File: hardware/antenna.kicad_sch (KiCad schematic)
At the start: 8 parts

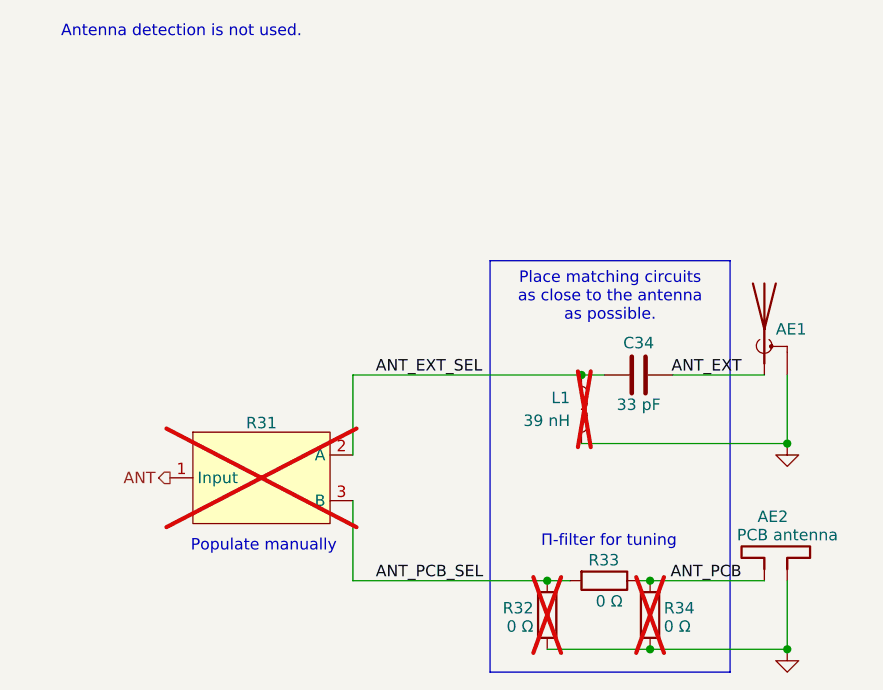
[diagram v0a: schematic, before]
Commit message: HW: Update 0hm choice
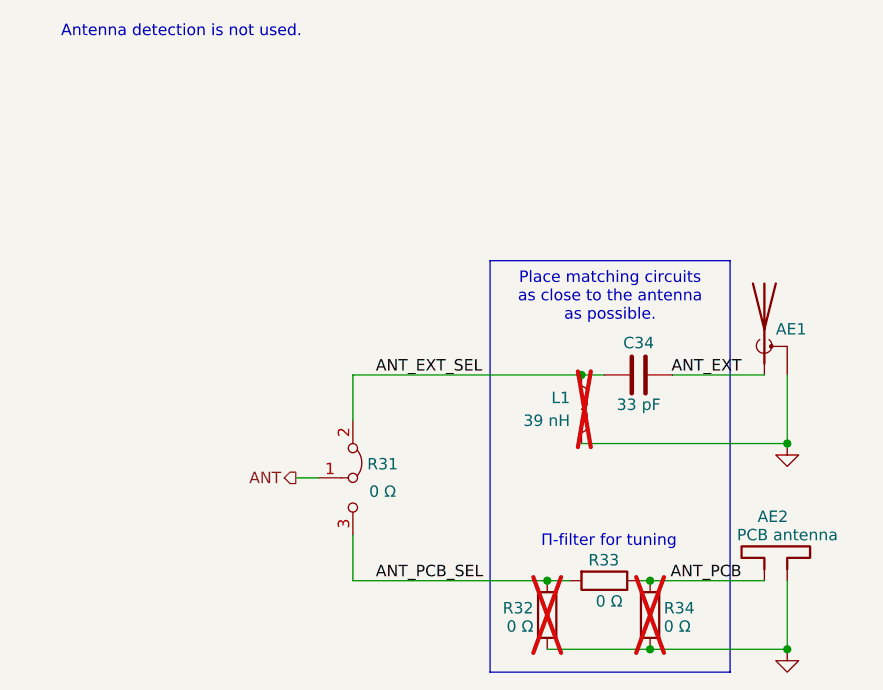
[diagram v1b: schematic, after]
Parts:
- R31: value ~ -> 0 Ω; now fitted; now in the parts list
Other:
- note removed: "Populate manually"
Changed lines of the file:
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@@
 	(wire
 		(pts
-			(xy 134.62 119.38) (xy 123.19 119.38)
+			(xy 101.6 106.68) (xy 101.6 111.76)
 		)
 		(stroke
@@
 	(wire
 		(pts
-			(xy 149.86 111.76) (xy 149.86 119.38)
+			(xy 134.62 119.38) (xy 123.19 119.38)
 		)
 		(stroke
@@
 	(wire
 		(pts
-			(xy 101.6 97.79) (xy 101.6 88.9)
+			(xy 149.86 111.76) (xy 149.86 119.38)
 		)
 		(stroke
@@
 	(wire
 		(pts
+			(xy 95.25 100.33) (xy 97.79 100.33)
+		)
+		(stroke
+			(width 0)
+			(type default)
+		)
+	)
+	(wire
+		(pts
 			(xy 149.86 96.52) (xy 127 96.52)
 		)
@@
 	(wire
 		(pts
-			(xy 147.32 111.76) (xy 134.62 111.76)
+			(xy 101.6 88.9) (xy 101.6 93.98)
 		)
 		(stroke
@@
 	(wire
 		(pts
-			(xy 125.73 111.76) (xy 123.19 111.76)
+			(xy 147.32 111.76) (xy 134.62 111.76)
 		)
 		(stroke
@@
 	(wire
 		(pts
-			(xy 101.6 88.9) (xy 127 88.9)
+			(xy 125.73 111.76) (xy 123.19 111.76)
 		)
 		(stroke
@@
 	(wire
 		(pts
-			(xy 147.32 88.9) (xy 137.16 88.9)
+			(xy 101.6 88.9) (xy 127 88.9)
 		)
 		(stroke
@@
 	(wire
 		(pts
-			(xy 101.6 111.76) (xy 101.6 102.87)
+			(xy 147.32 88.9) (xy 137.16 88.9)
 		)
 		(stroke
@@
 		)
 	)
-	(text "Populate manually"
-		(exclude_from_sim no)
-		(at 91.694 107.95 0)
-		(effects
-			(font
-				(size 1.27 1.27)
-			)
-		)
-	)
 	(text "Π-filter for tuning"
 		(exclude_from_sim no)
@@
 	(hierarchical_label "ANT"
 		(shape output)
-		(at 81.28 100.33 180)
+		(at 95.25 100.33 180)
 		(fields_autoplaced yes)
 		(effects
@@
 	(symbol
 		(lib_id "perfect_footprints:0hm_choice")
-		(at 91.44 100.33 0)
+		(at 101.6 100.33 270)
 		(unit 1)
 		(exclude_from_sim no)
-		(in_bom no)
+		(in_bom yes)
 		(on_board yes)
-		(dnp yes)
+		(dnp no)
 		(property "Reference" "R31"
-			(at 91.44 94.234 0)
+			(at 104.902 98.806 90)
 			(effects
 				(font
@@
 			)
 		)
-		(property "Value" "~"
-			(at 91.44 93.98 0)
+		(property "Value" "0 Ω"
+			(at 104.902 101.854 90)
 			(effects
 				(font
@@
 		)
 		(property "Footprint" "perfect_footprints:0hm_choice"
-			(at 91.44 108.458 0)
+			(at 93.472 100.33 0)
 			(effects
 				(font
@@
 		)
 		(property "Datasheet" ""
-			(at 86.36 96.52 0)
+			(at 105.41 95.25 0)
 			(effects
 				(font
@@
 		)
 		(property "Description" ""
-			(at 86.36 96.52 0)
+			(at 105.41 95.25 0)
 			(effects
 				(font

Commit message: HW: Update BOM
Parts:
- AE2: Digi-Key Part Number (none) -> -; Manufacturer (none) -> -; Manufacturer Part Number (none) -> -
- R31: Digi-Key Part Number (none) -> 311-0.0JRCT-ND; Manufacturer (none) -> YAGEO; Manufacturer Part Number (none) -> RC0402JR-070RL
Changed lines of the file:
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@@
+			)
+		)
+		(property "Digi-Key Part Number" "-"
+			(at 147.32 106.68 0)
+			(effects
+				(font
+					(size 1.27 1.27)
+				)
+				(hide yes)
+			)
+		)
+		(property "Manufacturer" "-"
+			(at 147.32 106.68 0)
+			(effects
+				(font
+					(size 1.27 1.27)
+				)
+				(hide yes)
+			)
+		)
+		(property "Manufacturer Part Number" "-"
+			(at 147.32 106.68 0)
+			(effects
+				(font
+					(size 1.27 1.27)
+				)
+				(hide yes)
 			)
 		)
@@
 			(effects
 				(font
+					(size 1.27 1.27)
+				)
+				(hide yes)
+			)
+		)
+		(property "Digi-Key Part Number" "311-0.0JRCT-ND"
+			(at 101.6 100.33 0)
+			(effects
+				(font
+					(size 1.27 1.27)
+				)
+				(hide yes)
+			)
+		)
+		(property "Manufacturer" "YAGEO"
+			(at 101.6 100.33 0)
+			(effects
+				(font
+					(size 1.27 1.27)
+				)
+				(hide yes)
+			)
+		)
+		(property "Manufacturer Part Number" "RC0402JR-070RL"
+			(at 101.6 100.33 0)
+			(effects
+				(font

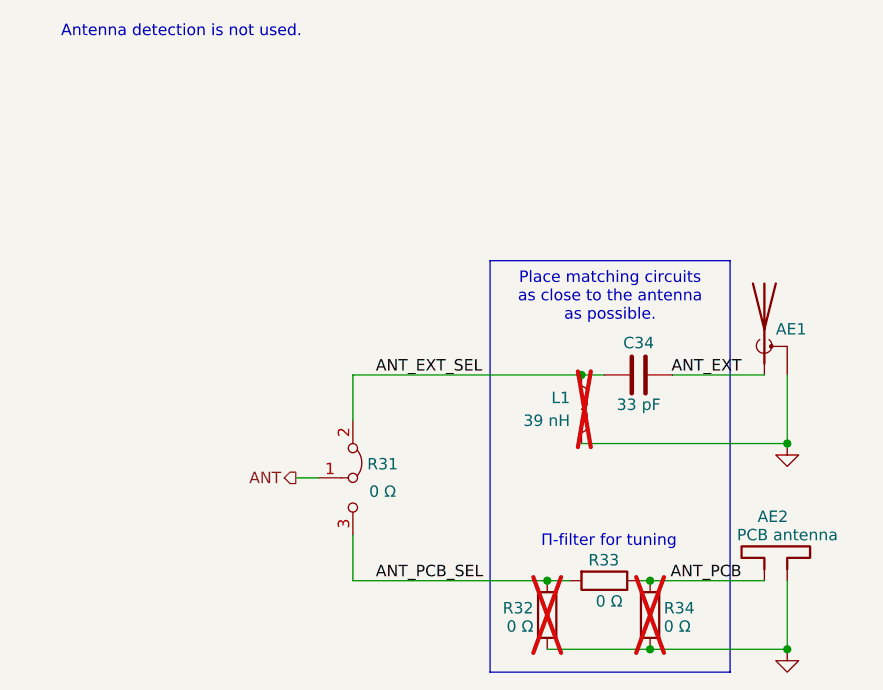
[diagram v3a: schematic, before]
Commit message: HW: Connect +BATT to MCU
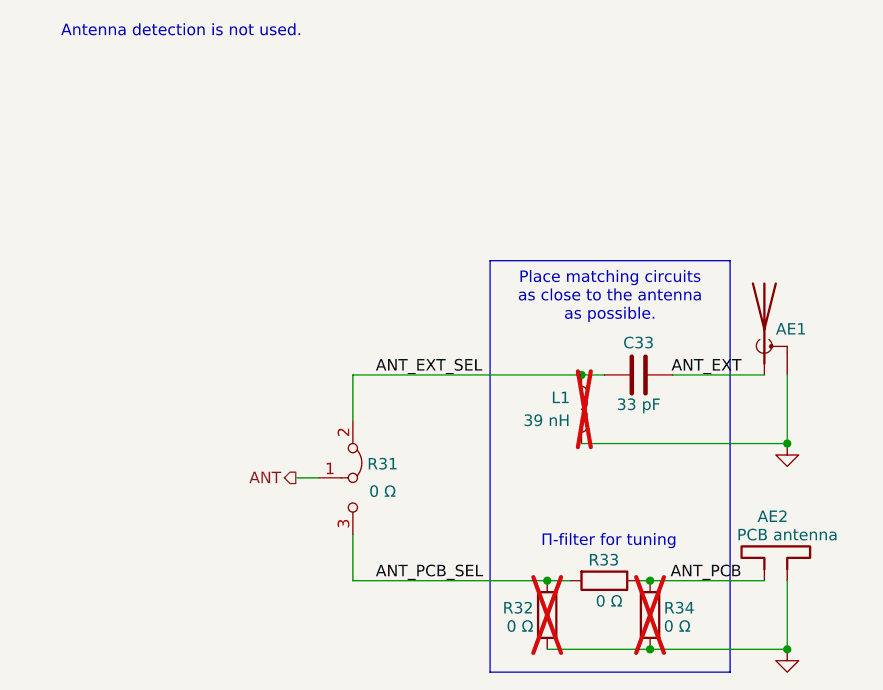
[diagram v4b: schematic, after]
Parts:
- renumbered C34 to C33
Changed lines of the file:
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@@
 	(title_block
 		(title "Iida devkit")
-		(date "2024-09-22")
-		(rev "v4.1.0")
+		(date "2024-09-25")
+		(rev "v4.2.0")
 	)
 	(junction
@@
 		(on_board yes)
 		(dnp no)
-		(property "Reference" "C34"
+		(property "Reference" "C33"
 			(at 133.35 85.344 90)
 			(effects
@@
 			(project "iida_devkit"
 				(path "/b12a6e25-97fb-4aba-bc96-af8db389bb9a/6e456e95-dbda-43fc-b148-815c3be21ba0"
-					(reference "C34")
+					(reference "C33")
 					(unit 1)
 				)

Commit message: HW: Update components
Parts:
- C33: Digi-Key Part Number 490-5936-1-ND -> 732-7472-1-ND; Manufacturer Murata Electronics -> Würth Elektronik; Manufacturer Part Number GRM1555C1H330JA01D -> 885012005058
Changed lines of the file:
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@@
 			)
 		)
-		(property "Digi-Key Part Number" "490-5936-1-ND"
+		(property "Digi-Key Part Number" "732-7472-1-ND"
 			(at 133.35 88.9 0)
 			(effects
@@
 			)
 		)
-		(property "Manufacturer" "Murata Electronics"
+		(property "Manufacturer" "Würth Elektronik"
 			(at 133.35 88.9 0)
 			(effects
@@
 			)
 		)
-		(property "Manufacturer Part Number" "GRM1555C1H330JA01D"
+		(property "Manufacturer Part Number" "885012005058"
 			(at 133.35 88.9 0)
 			(effects

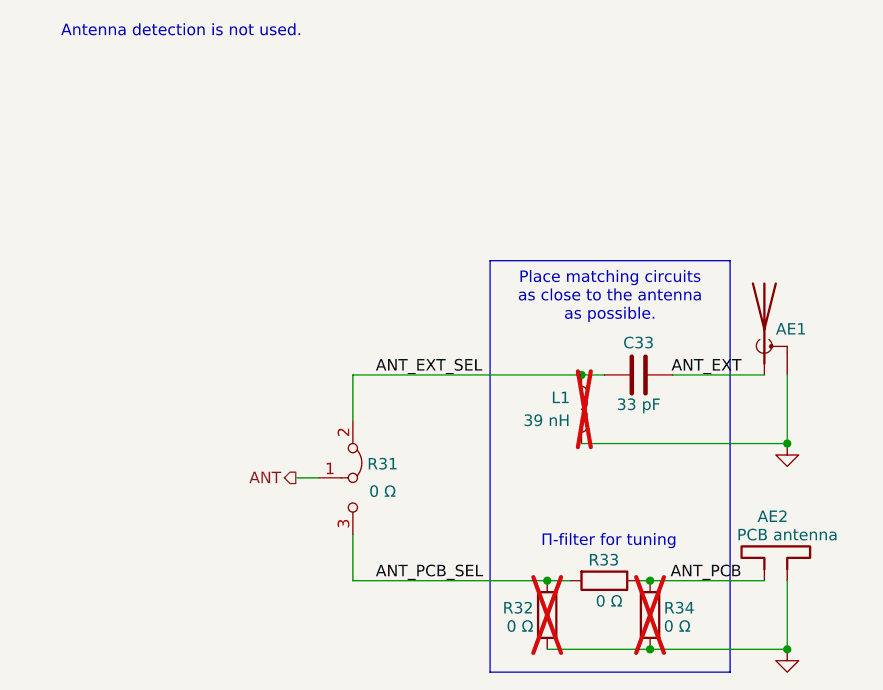
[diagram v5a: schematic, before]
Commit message: HW: Update VBAT, schema and layout
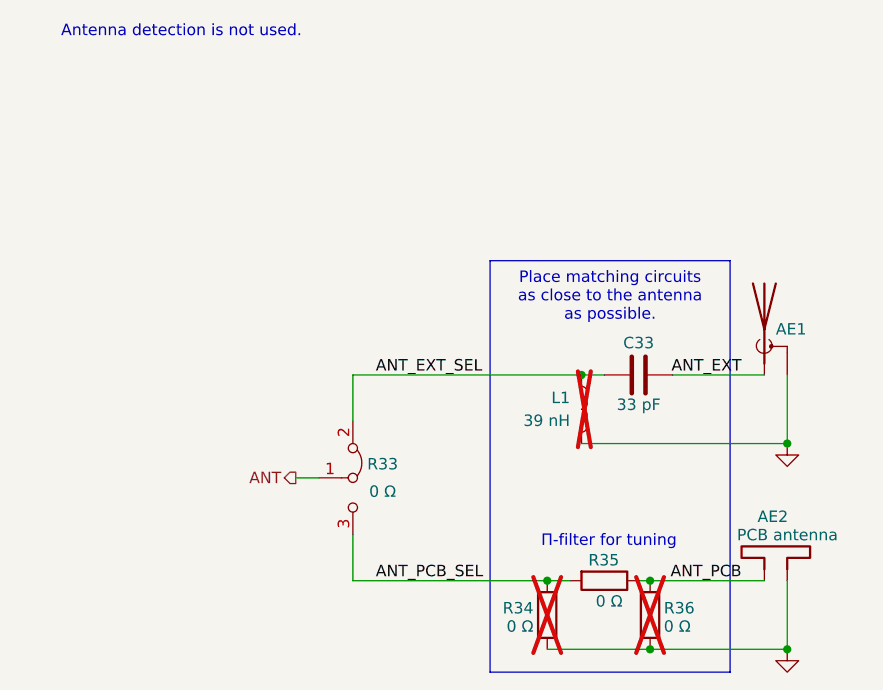
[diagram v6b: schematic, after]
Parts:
- renumbered R31 to R33, R32 to R34, R33 to R35, R34 to R36
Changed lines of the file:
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@@
 		(on_board yes)
 		(dnp no)
-		(property "Reference" "R33"
+		(property "Reference" "R35"
 			(at 127.762 109.474 90)
 			(effects
@@
 			(project "iida_devkit"
 				(path "/b12a6e25-97fb-4aba-bc96-af8db389bb9a/6e456e95-dbda-43fc-b148-815c3be21ba0"
-					(reference "R33")
+					(reference "R35")
 					(unit 1)
 				)
@@
 		(on_board yes)
 		(dnp yes)
-		(property "Reference" "R32"
+		(property "Reference" "R34"
 			(at 121.666 114.808 0)
 			(effects
@@
 			(project "iida_devkit"
 				(path "/b12a6e25-97fb-4aba-bc96-af8db389bb9a/6e456e95-dbda-43fc-b148-815c3be21ba0"
-					(reference "R32")
+					(reference "R34")
 					(unit 1)
 				)
@@
 		(on_board yes)
 		(dnp yes)
-		(property "Reference" "R34"
+		(property "Reference" "R36"
 			(at 136.144 114.808 0)
 			(effects
@@
 			(project "iida_devkit"
 				(path "/b12a6e25-97fb-4aba-bc96-af8db389bb9a/6e456e95-dbda-43fc-b148-815c3be21ba0"
-					(reference "R34")
+					(reference "R36")
 					(unit 1)
 				)
@@
 		(on_board yes)
 		(dnp no)
-		(property "Reference" "R31"
+		(property "Reference" "R33"
 			(at 104.902 98.806 90)
 			(effects
@@
 			(project ""
 				(path "/b12a6e25-97fb-4aba-bc96-af8db389bb9a/6e456e95-dbda-43fc-b148-815c3be21ba0"
-					(reference "R31")
+					(reference "R33")
 					(unit 1)
 				)

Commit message: HW: Start adding Li-Po support
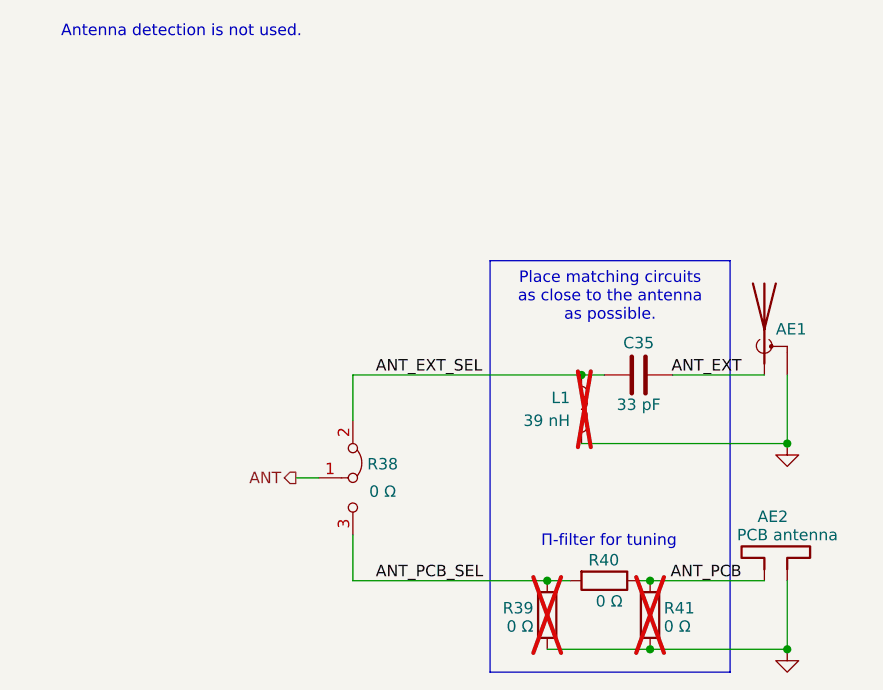
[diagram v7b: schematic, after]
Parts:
- renumbered C33 to C35, R33 to R38, R34 to R39, R35 to R40, R36 to R41
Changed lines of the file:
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@@
 		(on_board yes)
 		(dnp no)
-		(property "Reference" "C33"
+		(property "Reference" "C35"
 			(at 133.35 85.344 90)
 			(effects
@@
 			(project "iida_devkit"
 				(path "/b12a6e25-97fb-4aba-bc96-af8db389bb9a/6e456e95-dbda-43fc-b148-815c3be21ba0"
-					(reference "C33")
+					(reference "C35")
 					(unit 1)
 				)
@@
 		(on_board yes)
 		(dnp no)
-		(property "Reference" "R35"
+		(property "Reference" "R40"
 			(at 127.762 109.474 90)
 			(effects
@@
 			(project "iida_devkit"
 				(path "/b12a6e25-97fb-4aba-bc96-af8db389bb9a/6e456e95-dbda-43fc-b148-815c3be21ba0"
-					(reference "R35")
+					(reference "R40")
 					(unit 1)
 				)
@@
 		(dnp no)
 		(fields_autoplaced yes)
-		(property "Reference" "#PWR029"
+		(property "Reference" "#PWR051"
 			(at 149.86 125.73 0)
 			(effects
@@
 			(project "iida_devkit"
 				(path "/b12a6e25-97fb-4aba-bc96-af8db389bb9a/6e456e95-dbda-43fc-b148-815c3be21ba0"
-					(reference "#PWR029")
+					(reference "#PWR051")
 					(unit 1)
 				)
@@
 		(on_board yes)
 		(dnp yes)
-		(property "Reference" "R34"
+		(property "Reference" "R39"
 			(at 121.666 114.808 0)
 			(effects
@@
 			(project "iida_devkit"
 				(path "/b12a6e25-97fb-4aba-bc96-af8db389bb9a/6e456e95-dbda-43fc-b148-815c3be21ba0"
-					(reference "R34")
+					(reference "R39")
 					(unit 1)
 				)
@@
 		(on_board yes)
 		(dnp yes)
-		(property "Reference" "R36"
+		(property "Reference" "R41"
 			(at 136.144 114.808 0)
 			(effects
@@
 			(project "iida_devkit"
 				(path "/b12a6e25-97fb-4aba-bc96-af8db389bb9a/6e456e95-dbda-43fc-b148-815c3be21ba0"
-					(reference "R36")
+					(reference "R41")
 					(unit 1)
 				)
@@
 		(on_board yes)
 		(dnp no)
-		(property "Reference" "R33"
+		(property "Reference" "R38"
 			(at 104.902 98.806 90)
 			(effects
@@
 			(project ""
 				(path "/b12a6e25-97fb-4aba-bc96-af8db389bb9a/6e456e95-dbda-43fc-b148-815c3be21ba0"
-					(reference "R33")
+					(reference "R38")
 					(unit 1)
 				)
@@
 		(dnp no)
 		(fields_autoplaced yes)
-		(property "Reference" "#PWR028"
+		(property "Reference" "#PWR050"
 			(at 149.86 102.87 0)
 			(effects
@@
 			(project "iida_devkit"
 				(path "/b12a6e25-97fb-4aba-bc96-af8db389bb9a/6e456e95-dbda-43fc-b148-815c3be21ba0"
-					(reference "#PWR028")
-					(unit 1)
-				)
+					(reference "#PWR050")
+					(unit 1)
+				)

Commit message: HW: Replace STM QFN with QFP
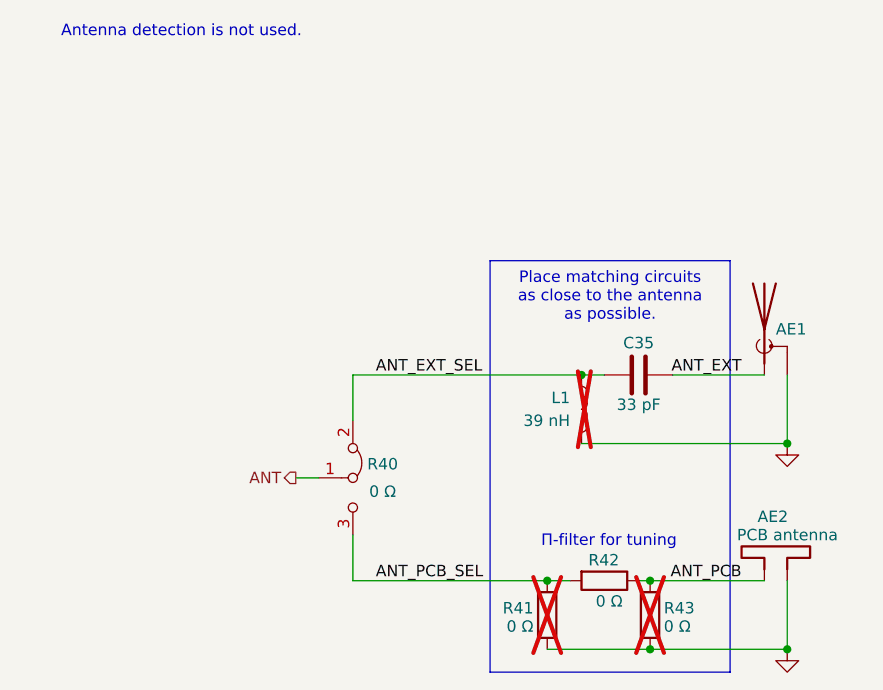
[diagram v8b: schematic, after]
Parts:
- renumbered R38 to R40, R39 to R41, R40 to R42, R41 to R43
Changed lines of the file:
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@@
 		(on_board yes)
 		(dnp no)
-		(property "Reference" "R40"
+		(property "Reference" "R42"
 			(at 127.762 109.474 90)
 			(effects
@@
 			(project "iida_devkit"
 				(path "/b12a6e25-97fb-4aba-bc96-af8db389bb9a/6e456e95-dbda-43fc-b148-815c3be21ba0"
-					(reference "R40")
+					(reference "R42")
 					(unit 1)
 				)
@@
 		(dnp no)
 		(fields_autoplaced yes)
-		(property "Reference" "#PWR051"
+		(property "Reference" "#PWR054"
 			(at 149.86 125.73 0)
 			(effects
@@
 			(project "iida_devkit"
 				(path "/b12a6e25-97fb-4aba-bc96-af8db389bb9a/6e456e95-dbda-43fc-b148-815c3be21ba0"
-					(reference "#PWR051")
+					(reference "#PWR054")
 					(unit 1)
 				)
@@
 		(on_board yes)
 		(dnp yes)
-		(property "Reference" "R39"
+		(property "Reference" "R41"
 			(at 121.666 114.808 0)
 			(effects
@@
 			(project "iida_devkit"
 				(path "/b12a6e25-97fb-4aba-bc96-af8db389bb9a/6e456e95-dbda-43fc-b148-815c3be21ba0"
-					(reference "R39")
+					(reference "R41")
 					(unit 1)
 				)
@@
 		(on_board yes)
 		(dnp yes)
-		(property "Reference" "R41"
+		(property "Reference" "R43"
 			(at 136.144 114.808 0)
 			(effects
@@
 			(project "iida_devkit"
 				(path "/b12a6e25-97fb-4aba-bc96-af8db389bb9a/6e456e95-dbda-43fc-b148-815c3be21ba0"
-					(reference "R41")
+					(reference "R43")
 					(unit 1)
 				)
@@
 		(on_board yes)
 		(dnp no)
-		(property "Reference" "R38"
+		(property "Reference" "R40"
 			(at 104.902 98.806 90)
 			(effects
@@
 			(project ""
 				(path "/b12a6e25-97fb-4aba-bc96-af8db389bb9a/6e456e95-dbda-43fc-b148-815c3be21ba0"
-					(reference "R38")
+					(reference "R40")
 					(unit 1)
 				)
@@
 		(dnp no)
 		(fields_autoplaced yes)
-		(property "Reference" "#PWR050"
+		(property "Reference" "#PWR053"
 			(at 149.86 102.87 0)
 			(effects
@@
 			(project "iida_devkit"
 				(path "/b12a6e25-97fb-4aba-bc96-af8db389bb9a/6e456e95-dbda-43fc-b148-815c3be21ba0"
-					(reference "#PWR050")
-					(unit 1)
-				)
+					(reference "#PWR053")
+					(unit 1)
+				)
